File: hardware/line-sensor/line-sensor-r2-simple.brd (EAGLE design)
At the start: 112 x 60 mm, 120 parts, among them IC1 GP2S60, IC10 GP2S60, IC11 GP2S60, IC12 GP2S60, IC13 GP2S60, IC14 GP2S60, IC15 GP2S60, IC16 GP2S60, IC17 GP2S60, IC18 GP2S60, IC19 GP2S60, IC2 GP2S60, IC20 GP2S60, IC21 GP2S60, IC22 GP2S60, IC23 GP2S60, IC24 GP2S60, IC25 GP2S60, IC26 STM32L151VE, IC27 TI-LM5165YDRCR, IC28 TI-TPS62170, IC29 AD-REF196GSZ, IC3 GP2S60, IC30 AD-ADP124ARHZ, IC4 GP2S60, IC5 GP2S60, IC6 GP2S60, IC7 GP2S60, IC8 GP2S60, IC9 GP2S60, J1 MOLEX-502382-02XX, J2 MOLEX-502382-05XX, J3 MOLEX-53261-0771

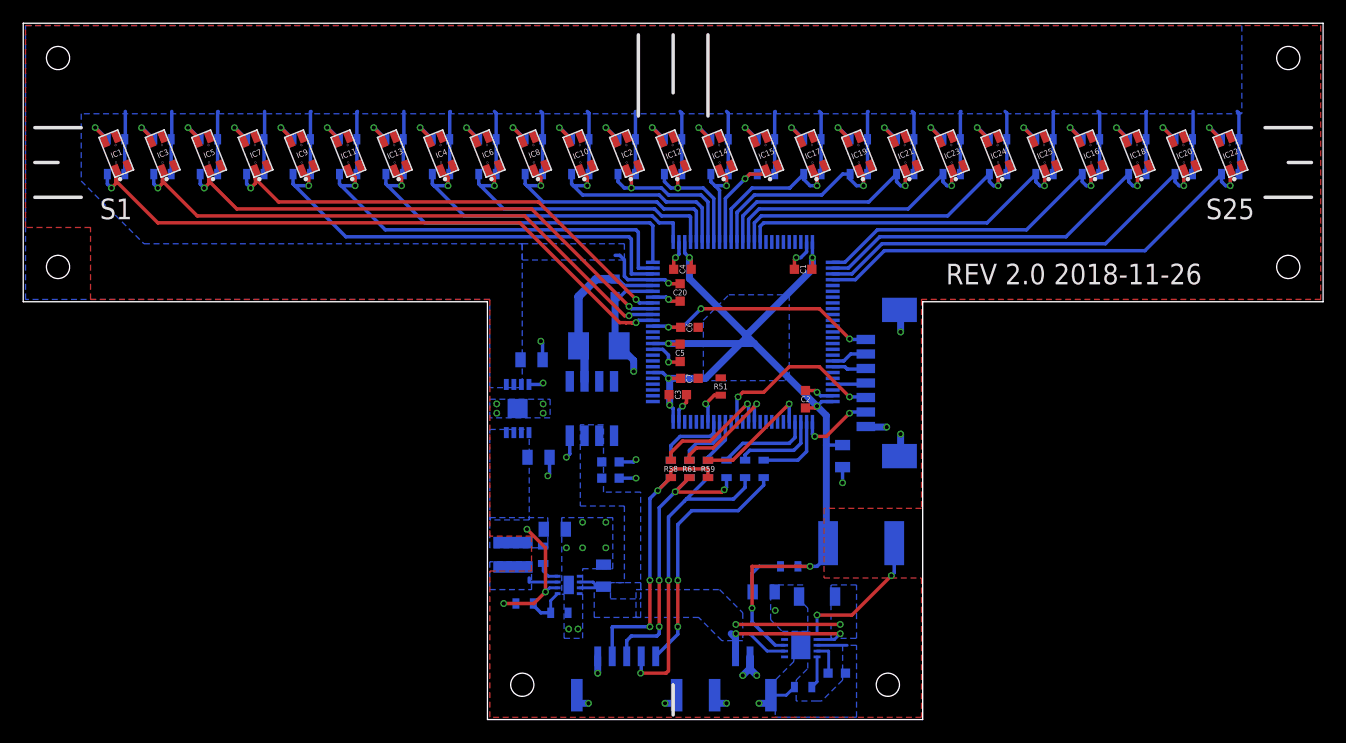
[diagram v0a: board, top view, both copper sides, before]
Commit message: - finished layout for line sensor with both linear and simple voltage sources (for testing)
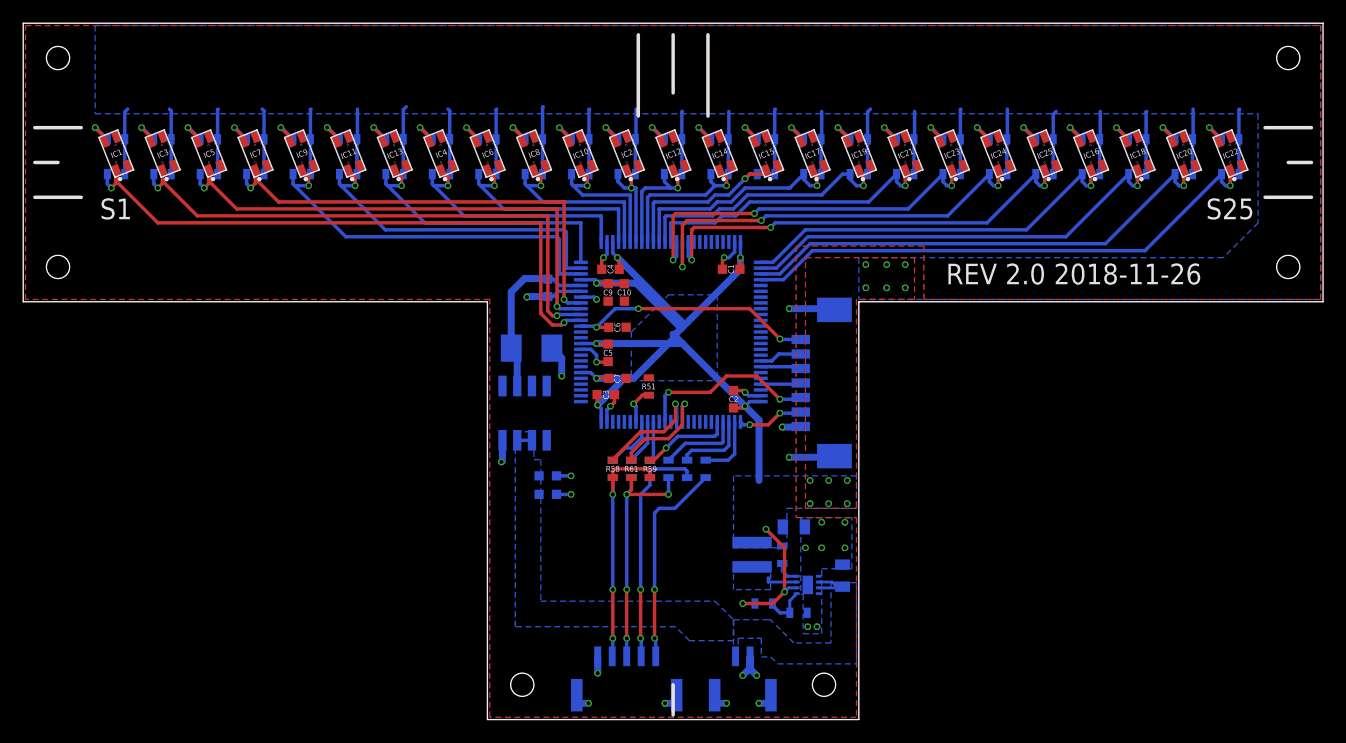
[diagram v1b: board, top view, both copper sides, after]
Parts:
- removed C11: 22u 10V X7S, capacitors:CAPACITOR-0805
- removed C12: 4.7u, capacitors:CAPACITOR-0805
- removed C15, C18: 1u 10V X7R, capacitors:CAPACITOR-0805
- removed C20: 0.1u 10V X7R, capacitors:CAPACITOR-0603
- removed IC27: TI-LM5165YDRCR, voltage-source:VSON-10-0.5MM
- removed IC30: AD-ADP124ARHZ, voltage-source:MSOP-8-EP
- removed L2: 150u 0.35A, inductors:ELL-6SH151M
- removed R52: 121k 1%, resistors:RESISTOR-0603
- removed R54: 0.5 1%, resistors:RESISTOR-0603
- C10: value 33n 10V X7R -> 1u
- C9: value 1u 50V X7R -> 0.1u; device capacitors:CAPACITOR-1206 -> capacitors:CAPACITOR-0603
- R55: value 610k 1% -> 562k 1%
- moved C10 37.6 mm to (75.8, 52.8), flipped to the top, turned to 270 degrees
- moved C9 31.8 mm to (74.4, 52.8), flipped to the top, turned to 270 degrees
- moved C13 20.6 mm to (90.4, 32.6)
- moved R53 20.6 mm to (89.4, 30.2)
- moved C8 20.6 mm to (94.6, 28.4)
- moved IC28 20.6 mm to (91.6, 27.6)
- moved L1 20.6 mm to (86.8, 30.2)
- moved R55 20.6 mm to (87.8, 26.0)
- moved R56 20.6 mm to (90.8, 25.2)
- moved C1 6.20 mm to (85.0, 54.8)
- moved C2 6.20 mm to (85.2, 43.6)
- moved C3 6.20 mm to (74.2, 44.0)
- moved C4 6.20 mm to (74.6, 54.8)
- moved C6 6.20 mm to (75.2, 49.8)
- moved C7 6.20 mm to (75.2, 45.4)
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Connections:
- removed net IC27_SW: IC27.1, L2.1
- removed net N$33: IC27.5, R52.P$1
- removed net N$34: C10.1, IC27.4
- removed net N$36: C11.1, R54.P$2
- removed net VDDA: C18.1, C20.1, IC26.22, IC30.1, IC30.2, IC30.3, R1.P$2, R10.P$2, R11.P$2, R12.P$2, R13.P$2, R14.P$2, R15.P$2, R16.P$2, R17.P$2, R18.P$2, R19.P$2, R2.P$2, R20.P$2, R21.P$2, R22.P$2, R23.P$2, R24.P$2, R25.P$2, R26.P$2, R27.P$2, R28.P$2, R29.P$2, R3.P$2, R30.P$2, R31.P$2, R32.P$2, R33.P$2, R34.P$2, R35.P$2, R36.P$2, R37.P$2, R38.P$2, R39.P$2, R4.P$2, R40.P$2, R41.P$2, R42.P$2, R43.P$2, R44.P$2, R45.P$2, R46.P$2, R47.P$2, R48.P$2, R49.P$2, R5.P$2, R50.P$2, R6.P$2, R7.P$2, R8.P$2, R9.P$2
- removed net VDDA3.5: C13.1, C15.1, IC28.6, IC30.5, IC30.7, IC30.8, L1.2, R53.P$2, R55.P$2
- net GND: now also C9.2; no longer C11.2, C12.2, C15.2, C18.2, C20.2, C9.P$2, IC27.10, IC27.11, IC27.3, IC30.4, IC30.PAD, R52.P$2
- net VBAT: no longer C9.P$1, IC27.2, IC27.7
- net VDD: now also C10.1, C13.1, C9.1, IC26.22, IC28.6, L1.2, R1.P$2, R10.P$2, R11.P$2, R12.P$2, R13.P$2, R14.P$2, R15.P$2, R16.P$2, R17.P$2, R18.P$2, R19.P$2, R2.P$2, R20.P$2, R21.P$2, R22.P$2, R23.P$2, R24.P$2, R25.P$2, R26.P$2, R27.P$2, R28.P$2, R29.P$2, R3.P$2, R30.P$2, R31.P$2, R32.P$2, R33.P$2, R34.P$2, R35.P$2, R36.P$2, R37.P$2, R38.P$2, R39.P$2, R4.P$2, R40.P$2, R41.P$2, R42.P$2, R43.P$2, R44.P$2, R45.P$2, R46.P$2, R47.P$2, R48.P$2, R49.P$2, R5.P$2, R50.P$2, R53.P$2, R55.P$2, R6.P$2, R7.P$2, R8.P$2, R9.P$2; no longer C12.1, IC27.8, L2.2, R54.P$1
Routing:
- net VDDA: track 143.4 -> 0.00 mm, vias 1 -> 0
- net VDD: track 90.6 -> 232.6 mm, vias 8 -> 22
- net VBAT: track 31.1 -> 5.22 mm, vias 4 -> 0
- net GND: track 63.1 -> 49.3 mm, vias 36 -> 28
- net VDDA3.5: track 12.3 -> 0.00 mm, vias 3 -> 0
- net IC27_SW: track 12.3 -> 0.00 mm, vias 2 -> 0
- net SENSOR_20: track 26.5 -> 36.9 mm, vias 1 -> 3
- net SENSOR_19: track 23.2 -> 33.1 mm, vias 1 -> 3
- net SENSOR_21: track 29.8 -> 38.8 mm, vias 1 -> 3
- net N$28: track 28.3 -> 20.2 mm
- net SENSOR_23: track 31.7 -> 37.9 mm
- net SENSOR_5: track 39.6 -> 33.4 mm
- net SENSOR_25: track 40.1 -> 46.3 mm
- net SENSOR_24: track 35.9 -> 42.1 mm
- net SENSOR_16: track 13.6 -> 19.8 mm
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- added copper zone on layer 1, net VDD
- removed copper zone on layer 16, net VDDA
- removed copper zone on layer 16, net VDDA3.5
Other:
- outline, holes or cut-outs redrawn
